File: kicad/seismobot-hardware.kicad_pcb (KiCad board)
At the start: 4 copper layers, 110 x 111 mm, 98 parts, among them J1 Screw_Terminal_01x02, J2 Raspberry_Pi_2_3, U1 OPA2156xD, U10 AP7340, U2 OPA2156xD, U3 ref-6, U4 ref-8, U5 LTC6011, U6 OPA2156xD, U7 OPA2156xD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

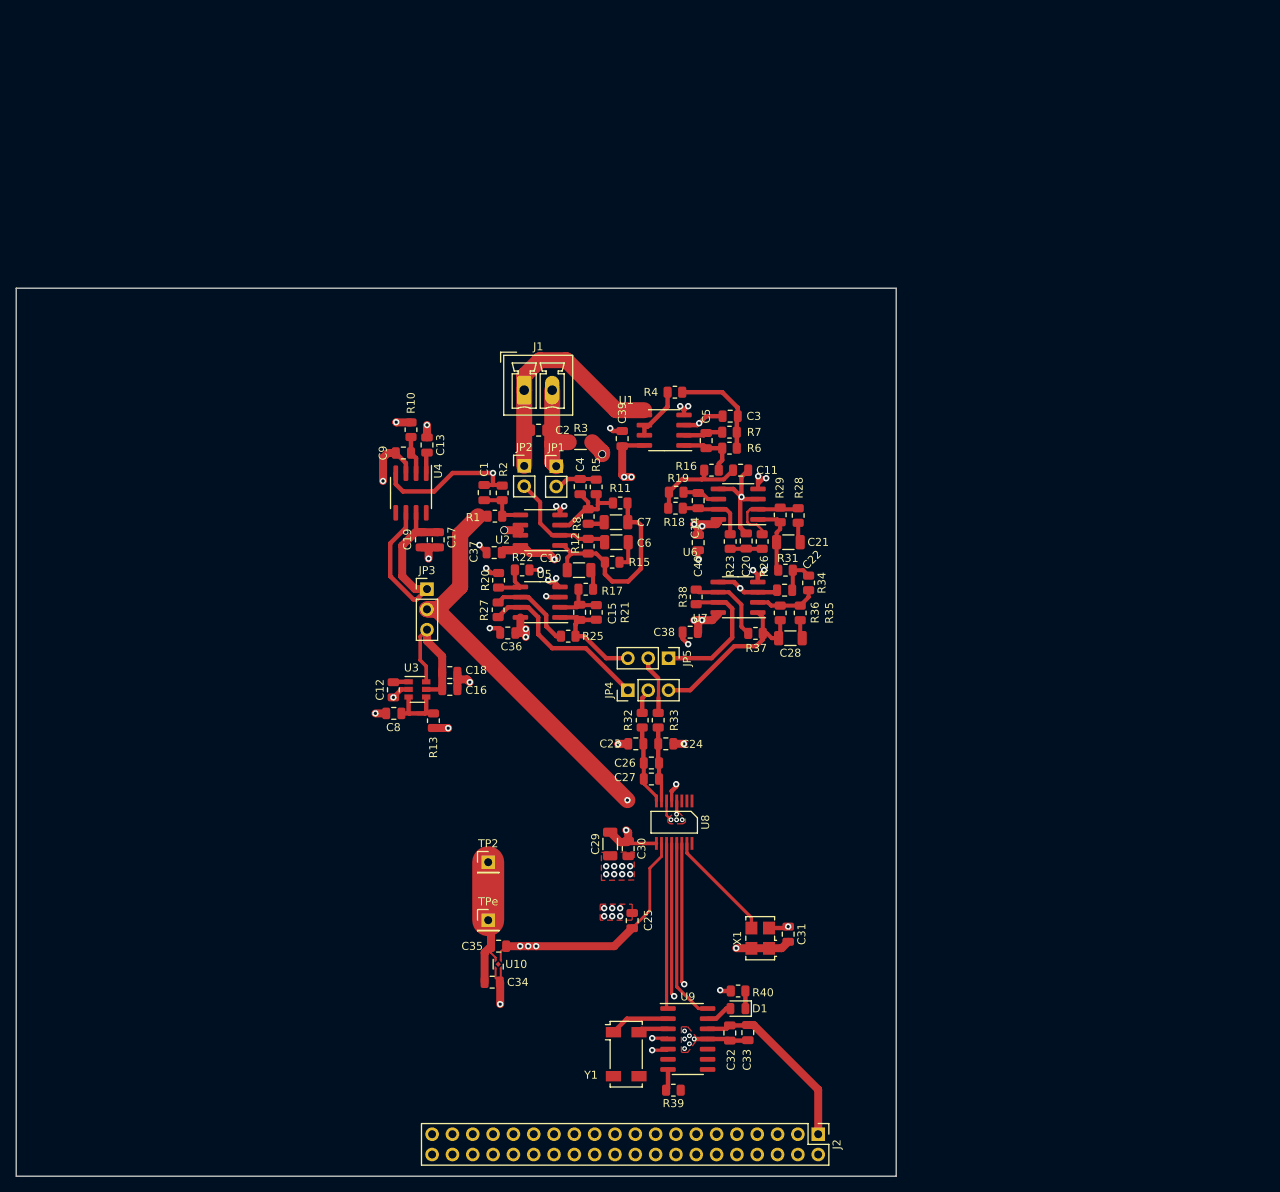
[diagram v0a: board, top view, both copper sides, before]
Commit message: add 3v3 power led
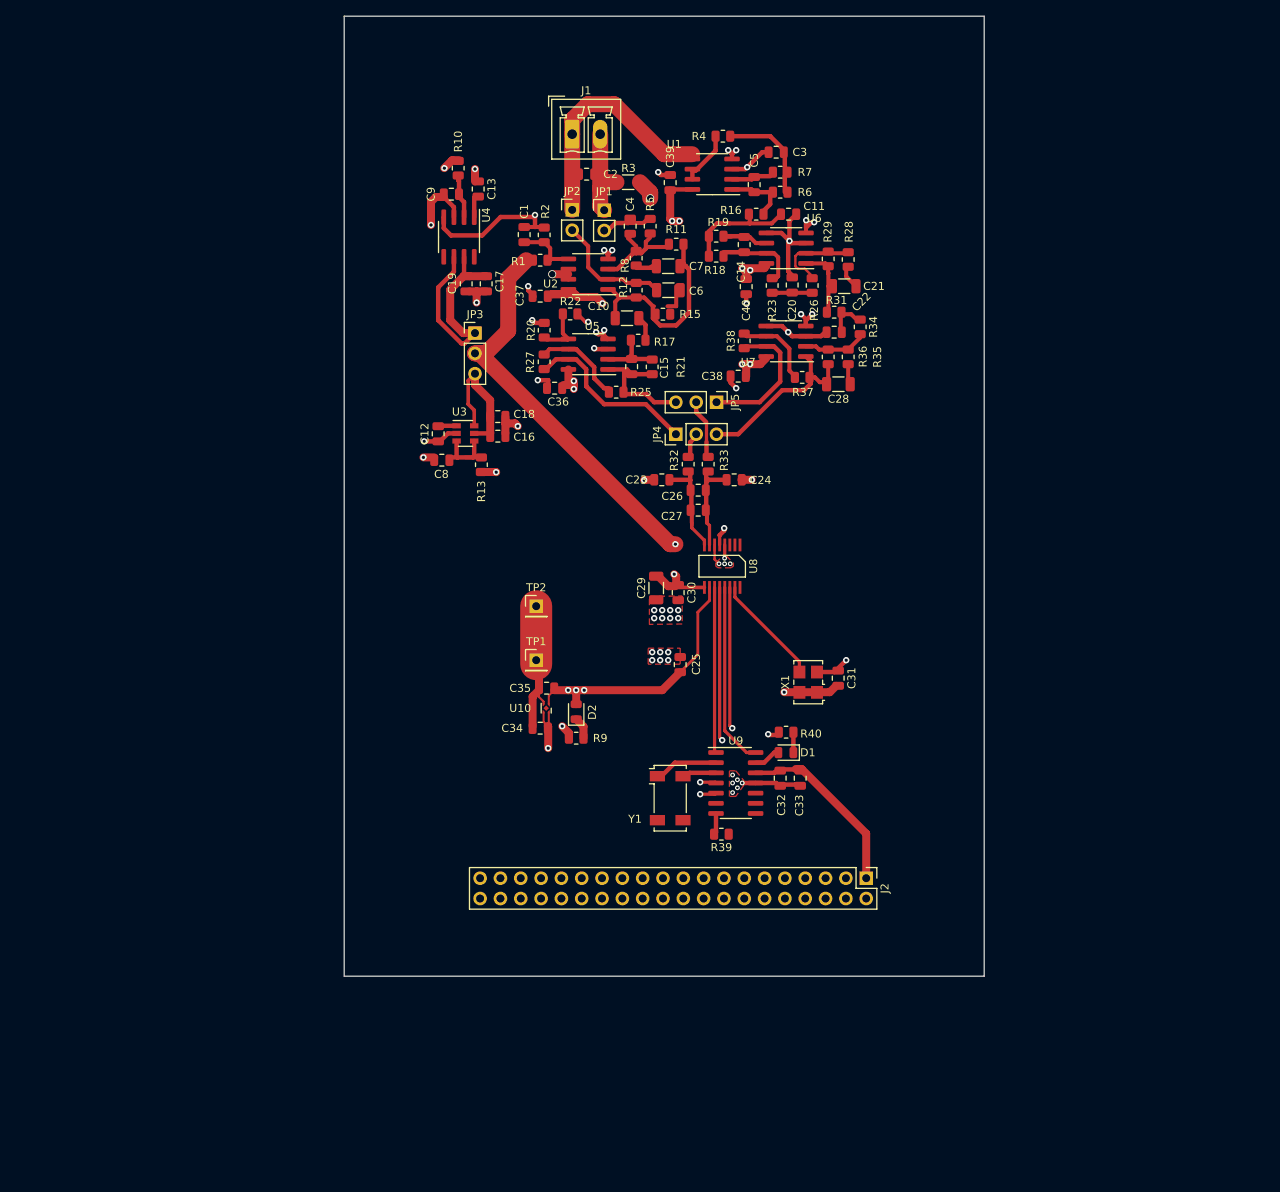
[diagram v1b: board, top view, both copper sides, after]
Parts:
- added D2: LED, LED_SMD:LED_0805_2012Metric, F.Cu at (129.0, 136.9)
- added R9: 100, Resistor_SMD:R_0805_2012Metric, F.Cu at (129.0, 140.2)
- moved C26 34.6 mm to (144.2, 109.2)
- moved C27 34.1 mm to (144.2, 111.8)
- moved C24 34.1 mm to (148.8, 108.0)
- moved C3 33.5 mm to (154.0, 67.0)
- moved R5 33.3 mm to (138.2, 76.2)
- moved R10 33.2 mm to (114.2, 69.0)
- moved C23 33.2 mm to (139.7, 108.0)
- moved C4 33.1 mm to (135.8, 76.2)
- moved R7 33.1 mm to (154.5, 69.5)
- moved R11 33.1 mm to (141.5, 78.5)
- moved TP1 33.0 mm to (124.0, 130.5)
- moved R3 33.0 mm to (135.5, 70.8)
- moved C9 32.9 mm to (113.4, 72.2)
- moved R40 32.9 mm to (155.2, 139.5)
- moved C22 32.8 mm to (161.2, 89.5)
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- renumbered TPe to TP1
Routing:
- net GND: track 96.5 -> 103.4 mm, vias 51 -> 52
- net Net-(C14-Pad1): track 4.72 -> 8.35 mm
- net Net-(C14-Pad2): track 8.80 -> 12.0 mm
- net +3V3: track 109.5 -> 112.5 mm
- net Net-(D2-Pad1): track 0.00 -> 2.75 mm
- net Net-(C24-Pad2): track 9.44 -> 12.1 mm
- net Net-(C23-Pad1): track 10.3 -> 12.9 mm
- net Net-(C4-Pad1): track 5.42 -> 7.01 mm
- net Net-(C15-Pad1): track 6.69 -> 8.24 mm
- net OUTa-: track 14.6 -> 16.0 mm
- net Net-(C4-Pad2): track 12.7 -> 14.0 mm
- net Net-(C11-Pad2): track 12.5 -> 13.7 mm
- net 1.5v: track 106.1 -> 107.1 mm
- net Net-(R20-Pad1): track 5.18 -> 6.18 mm
- net Net-(C20-Pad2): track 4.00 -> 4.75 mm
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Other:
- board size 110 x 111 mm -> 80 x 120 mm

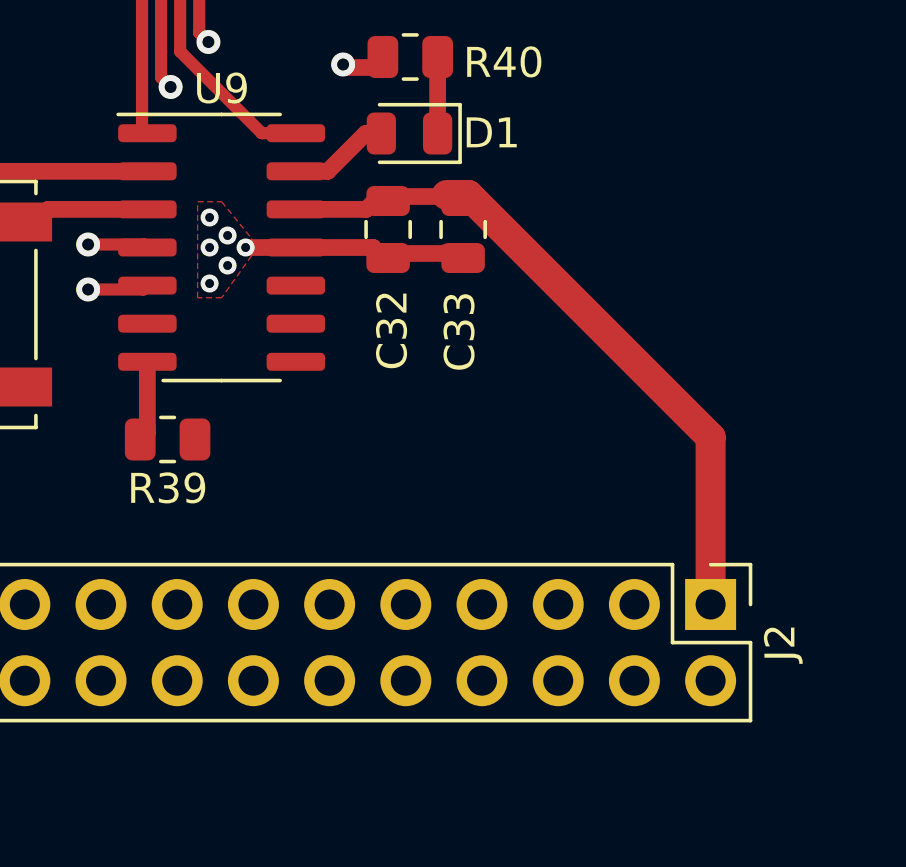
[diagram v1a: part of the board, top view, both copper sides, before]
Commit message: resize board
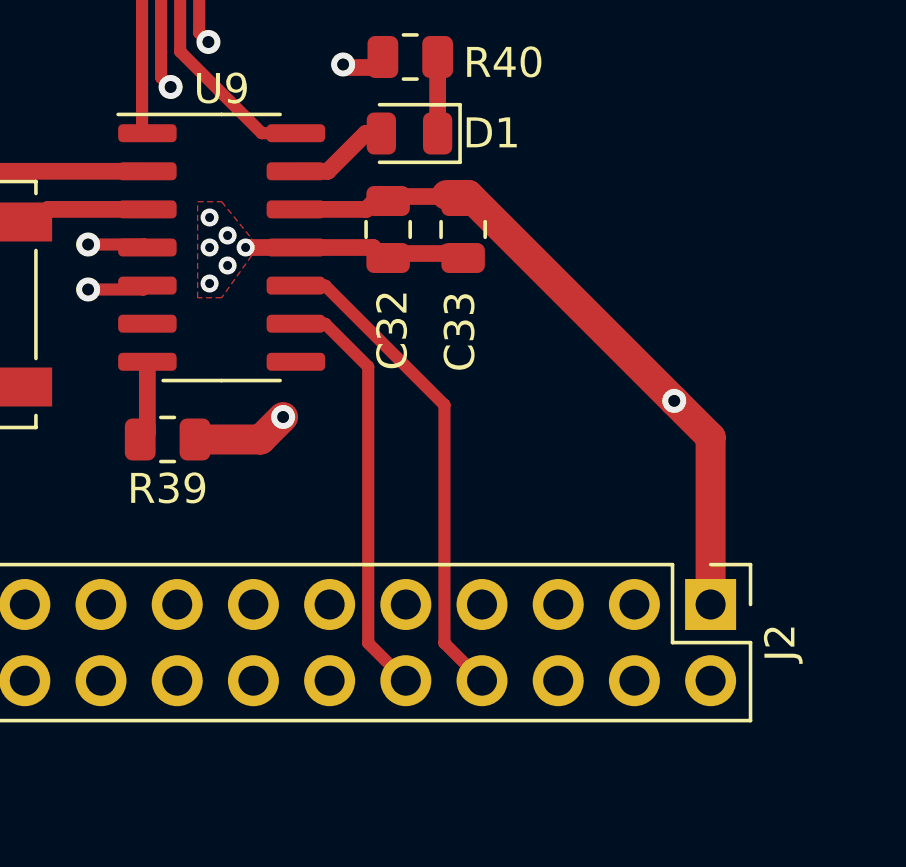
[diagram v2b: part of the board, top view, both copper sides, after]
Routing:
- net VDD: track 22.9 -> 39.5 mm, vias 0 -> 2
- net RxD: track 0.00 -> 16.3 mm
- net TxD: track 0.00 -> 14.0 mm
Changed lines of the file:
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@@
     (thickness 1.6)
     (drawings 6)
-    (tracks 653)
+    (tracks 669)
     (zones 0)
     (modules 100)
@@
   (gr_line (start 100 170) (end 180 170) (layer Edge.Cuts) (width 0.05))
   (gr_line (start 100 50) (end 100 170) (layer Edge.Cuts) (width 0.05))
-  (gr_text "Josh is thee best" (at 175.2 153) (layer B.SilkS)
+  (gr_text "Josh is thee best" (at 178 133.5) (layer B.SilkS)
     (effects (font (size 1.5 1.5) (thickness 0.3)))
   )
@@
   (segment (start 152.49 143.31) (end 153.75 142.05) (width 0.5588) (layer F.Cu) (net 28))
   (segment (start 156.15 142.05) (end 156.15 139.85) (width 0.5588) (layer F.Cu) (net 29))
+  (segment (start 153.836799 159.036799) (end 155.09 160.29) (width 0.4064) (layer F.Cu) (net 54))
+  (segment (start 153.836799 149.826799) (end 153.836799 159.036799) (width 0.4064) (layer F.Cu) (net 54))
+  (segment (start 152.4 148.39) (end 153.836799 149.826799) (width 0.4064) (layer F.Cu) (net 54))
+  (segment (start 151.425 148.39) (end 152.4 148.39) (width 0.4064) (layer F.Cu) (net 54))
+  (segment (start 156.376799 159.036799) (end 157.63 160.29) (width 0.4064) (layer F.Cu) (net 55))
+  (segment (start 156.376799 151.096799) (end 156.376799 159.036799) (width 0.4064) (layer F.Cu) (net 55))
+  (segment (start 152.4 147.12) (end 156.376799 151.096799) (width 0.4064) (layer F.Cu) (net 55))
+  (segment (start 151.425 147.12) (end 152.4 147.12) (width 0.4064) (layer F.Cu) (net 55))
   (via (at 147.5 114) (size 0.8) (drill 0.4) (layers F.Cu B.Cu) (net 60))
   (segment (start 146.9325 116.095) (end 146.9325 114.8886) (width 0.4064) (layer F.Cu) (net 60))
@@
   (segment (start 154.2 144.15) (end 156.4 144.15) (width 0.5588) (layer F.Cu) (net 96))
   (segment (start 165.25 152.175) (end 165.25 157.75) (width 1) (layer F.Cu) (net 96))
-  (segment (start 157.175 144.1) (end 165.25 152.175) (width 1) (layer F.Cu) (net 96))
   (segment (start 156.45 144.1) (end 157.175 144.1) (width 1) (layer F.Cu) (net 96))
+  (via (at 151 151.5) (size 0.8) (drill 0.4) (layers F.Cu B.Cu) (net 96))
+  (segment (start 150.25 152.25) (end 151 151.5) (width 1) (layer F.Cu) (net 96))
+  (segment (start 148.0625 152.25) (end 150.25 152.25) (width 1) (layer F.Cu) (net 96))
+  (segment (start 151 151.5) (end 151.5 151) (width 1) (layer In2.Cu) (net 96))
+  (segment (start 164 151) (end 164.0375 150.9625) (width 1) (layer In2.Cu) (net 96))
+  (via (at 164.0375 150.9625) (size 0.8) (drill 0.4) (layers F.Cu B.Cu) (net 96))
+  (segment (start 151.5 151) (end 164 151) (width 1) (layer In2.Cu) (net 96))
+  (segment (start 164.0375 150.9625) (end 165.25 152.175) (width 1) (layer F.Cu) (net 96))
+  (segment (start 157.175 144.1) (end 164.0375 150.9625) (width 1) (layer F.Cu) (net 96))
   (segment (start 129.9125 138.7875) (end 129.9125 140.25) (width 1) (layer F.Cu) (net 98))
   (segment (start 129 137.875) (end 129.9125 138.7875) (width 1) (layer F.Cu) (net 98))
@@
     (polygon
       (pts
-        (xy 171 163) (xy 111 163) (xy 111 129) (xy 171 129)
+        (xy 174.5 163) (xy 106 163) (xy 106 129) (xy 174.5 129)
       )
     )

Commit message: finishing touches before sending out rev 1
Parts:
- added J3: Conn_01x06_Male, Connector_PinHeader_2.54mm:PinHeader_1x06_P2.54mm_Horizontal, F.Cu at (183.0, 81.2)
- added R14: DNP, Resistor_SMD:R_0805_2012Metric, F.Cu at (113.5, 119.7)
- moved J2 82.1 mm to (202.8, 84.8), turned to 0 degrees
- moved R39 70.4 mm to (197.2, 102.8), turned to 270 degrees
- moved R10 66.8 mm to (114.0, 135.8), turned to 0 degrees
- moved Y1 64.7 mm to (192.8, 109.2), turned to 90 degrees
- moved C9 64.5 mm to (117.2, 136.6), turned to 90 degrees
- moved C33 61.9 mm to (190.2, 93.0), turned to 0 degrees
- moved C13 61.7 mm to (116.6, 133.2), turned to 0 degrees
- moved U9 61.3 mm to (190.8, 101.0), turned to 90 degrees
- moved C32 61.3 mm to (190.2, 95.5), turned to 180 degrees
- moved C34 61.0 mm to (184.0, 125.5), turned to 270 degrees
- moved J1 60.2 mm to (108.5, 121.5), turned to 90 degrees
- moved R9 59.5 mm to (185.2, 121.0), turned to 90 degrees
- moved U4 58.6 mm to (122.6, 135.7), turned to 0 degrees
- moved U10 57.5 mm to (181.5, 124.8), turned to 0 degrees
- moved D1 57.0 mm to (187.1, 94.8), turned to 270 degrees
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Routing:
- net SWCLK: track 2.69 -> 31.5 mm, vias 0 -> 1
- net ~RST: track 0.00 -> 26.8 mm, vias 0 -> 2
- net SWDIO: track 0.00 -> 25.0 mm, vias 0 -> 1
- net +3V3: track 112.5 -> 135.8 mm, vias 16 -> 21
- net VDD: track 39.5 -> 54.1 mm, vias 2 -> 3
- net G-: track 29.7 -> 31.6 mm
- net GND: track 103.4 -> 103.9 mm
- net (no net): vias 0 -> 4
- added copper zone on B.Cu, net (none)
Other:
- board size 80 x 120 mm -> 120 x 80 mm
- board text added: "Interstitial Tech + HomeDots"
- board text added: "July 2021"
- board text added: "Seismobot v0.1"
- board text added: "These additions were written by resident shepherds and guardians of the Bay Area Makerfarm:"
- board text added: "[thank you, marie]"
